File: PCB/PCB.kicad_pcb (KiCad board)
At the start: 4 copper layers, 54 x 29 mm, 108 parts, among them J1 USB_B_Micro, J2 Conn_01x02, Q1 PJA3428, Q2 PJA3428, Q3 AO3401A, SW1 SW_Push, SW2 SW_Push, SW3 SW_Push, SW4 ON/OFF, U1 ESP32-PICO-MINI-02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

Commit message: minor changes
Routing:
- net JTAG_TDI: track 0.00 -> 7.49 mm, vias 0 -> 1
- net JTAG_TDO: track 0.00 -> 5.23 mm, vias 0 -> 1
- net GPIO0: track 26.8 -> 27.6 mm
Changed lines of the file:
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@@
   (via (at 224.967457 102.491185) (size 0.8) (drill 0.4) (layers "F.Cu" "B.Cu") (net 8))
   (via (at 210.58 104.74) (size 0.8) (drill 0.4) (layers "F.Cu" "B.Cu") (net 8))
-  (segment (start 212.42 103.95) (end 211.81 103.95) (width 0.2) (layer "B.Cu") (net 8))
-  (segment (start 211.09 104.67) (end 211.02 104.74) (width 0.2) (layer "B.Cu") (net 8))
-  (segment (start 222.94 103.95) (end 212.42 103.95) (width 0.2) (layer "B.Cu") (net 8))
+  (segment (start 210.58 104.81) (end 211.479119 105.709119) (width 0.2) (layer "B.Cu") (net 8))
+  (segment (start 215.09387 104.16) (end 222.73 104.16) (width 0.2) (layer "B.Cu") (net 8))
+  (segment (start 210.58 104.74) (end 210.58 104.81) (width 0.2) (layer "B.Cu") (net 8))
+  (segment (start 211.479119 105.709119) (end 213.544751 105.709119) (width 0.2) (layer "B.Cu") (net 8))
   (segment (start 223.96 102.93) (end 224.528642 102.93) (width 0.2) (layer "B.Cu") (net 8))
   (segment (start 226.05 104.49) (end 225.52 104.49) (width 0.2) (layer "B.Cu") (net 8))
   (segment (start 224.528642 102.93) (end 224.967457 102.491185) (width 0.2) (layer "B.Cu") (net 8))
-  (segment (start 223.96 102.93) (end 223.27 103.62) (width 0.2) (layer "B.Cu") (net 8))
   (segment (start 225.52 104.49) (end 223.96 102.93) (width 0.2) (layer "B.Cu") (net 8))
-  (segment (start 223.27 103.62) (end 222.94 103.95) (width 0.2) (layer "B.Cu") (net 8))
-  (segment (start 211.02 104.74) (end 210.58 104.74) (width 0.2) (layer "B.Cu") (net 8))
-  (segment (start 211.81 103.95) (end 211.09 104.67) (width 0.2) (layer "B.Cu") (net 8))
+  (segment (start 213.544751 105.709119) (end 215.09387 104.16) (width 0.2) (layer "B.Cu") (net 8))
+  (segment (start 222.73 104.16) (end 223.96 102.93) (width 0.2) (layer "B.Cu") (net 8))
   (segment (start 228.785 106.13) (end 227.435 107.48) (width 0.2) (layer "B.Cu") (net 9))
   (segment (start 227.985 109.105) (end 228.485 109.105) (width 0.2) (layer "B.Cu") (net 9))
@@
   (segment (start 193.975 117.405) (end 193.28 118.1) (width 0.2) (layer "B.Cu") (net 87))
   (segment (start 193.975 116.85) (end 193.975 117.405) (width 0.2) (layer "B.Cu") (net 87))
+  (segment (start 213.79 103.4225) (end 213.79 104.394307) (width 0.2) (layer "F.Cu") (net 88))
+  (segment (start 213.79 104.394307) (end 213.175188 105.009119) (width 0.2) (layer "F.Cu") (net 88))
+  (via (at 213.175188 105.009119) (size 0.8) (drill 0.4) (layers "F.Cu" "B.Cu") (net 88))
+  (segment (start 213.8 104.107107) (end 213.888554 104.018554) (width 0.2) (layer "B.Cu") (net 88))
+  (segment (start 213.888554 104.018554) (end 215.245 102.662107) (width 0.2) (layer "B.Cu") (net 88))
+  (segment (start 213.175188 105.009119) (end 213.175188 104.73192) (width 0.2) (layer "B.Cu") (net 88))
+  (segment (start 213.175188 104.73192) (end 213.888554 104.018554) (width 0.2) (layer "B.Cu") (net 88))
+  (segment (start 215.245 101.33) (end 214.545 100.63) (width 0.2) (layer "B.Cu") (net 88))
+  (segment (start 215.245 102.662107) (end 215.245 101.33) (width 0.2) (layer "B.Cu") (net 88))
   (segment (start 212.99 102.275) (end 214.515 100.75) (width 0.2) (layer "F.Cu") (net 89))
   (segment (start 212.99 103.4225) (end 212.99 102.275) (width 0.2) (layer "F.Cu") (net 89))
@@
   (segment (start 215.215 99.92) (end 214.515 99.22) (width 0.2) (layer "F.Cu") (net 90))
   (segment (start 214.59 101.857107) (end 215.215 101.232107) (width 0.2) (layer "F.Cu") (net 90))
+  (segment (start 212.19 104.78) (end 212.2 104.79) (width 0.2) (layer "F.Cu") (net 91))
+  (segment (start 212.19 103.4225) (end 212.19 104.78) (width 0.2) (layer "F.Cu") (net 91))
+  (via (at 212.2 104.79) (size 0.8) (drill 0.4) (layers "F.Cu" "B.Cu") (net 91))
+  (segment (start 214.077107 102.18) (end 214.545 102.18) (width 0.2) (layer "B.Cu") (net 91))
+  (segment (start 212.2 104.79) (end 212.2 104.057107) (width 0.2) (layer "B.Cu") (net 91))
+  (segment (start 212.2 104.057107) (end 214.077107 102.18) (width 0.2) (layer "B.Cu") (net 91))
   (segment (start 212.432547 101.092453) (end 211.422453 101.092453) (width 0.2) (layer "B.Cu") (net 92))
   (segment (start 192.77 101.1) (end 192.77 100.3) (width 0.2) (layer "B.Cu") (net 92))

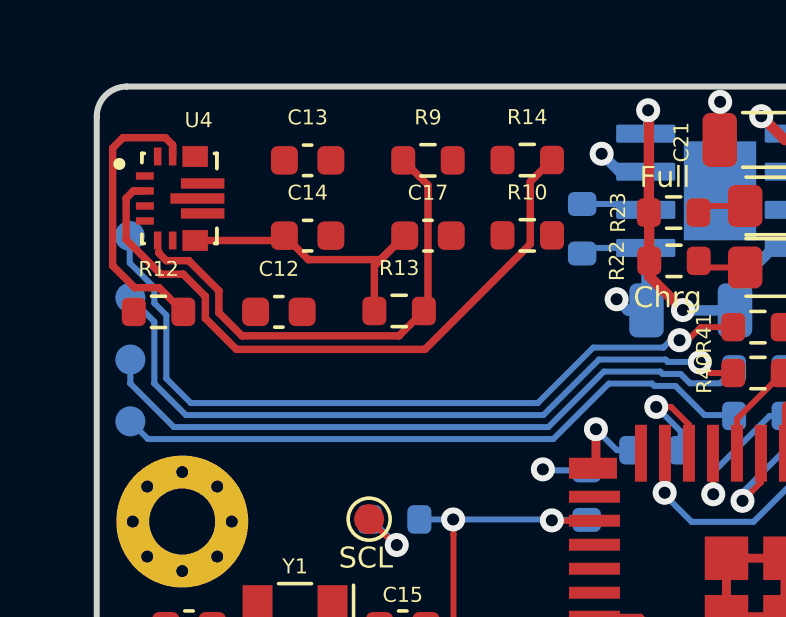
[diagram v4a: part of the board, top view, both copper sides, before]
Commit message: buck-boost pcb
layout updated
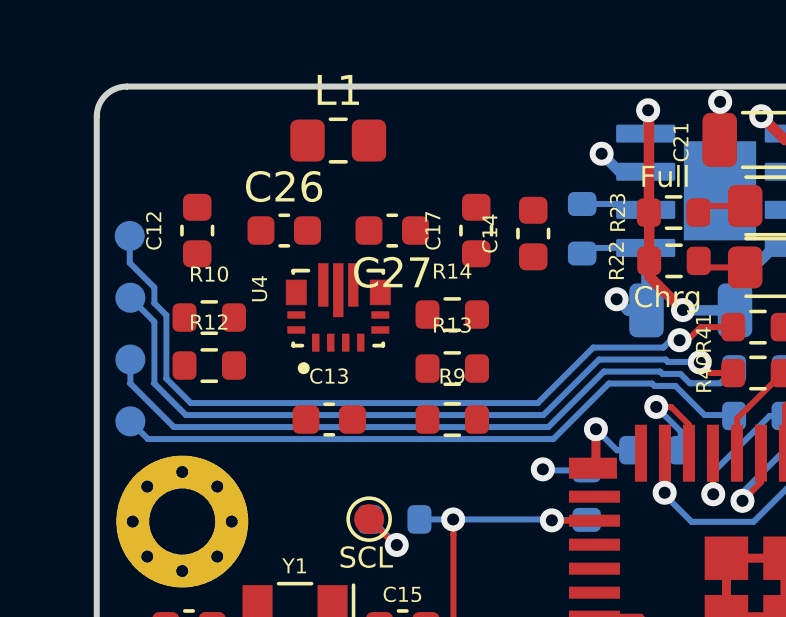
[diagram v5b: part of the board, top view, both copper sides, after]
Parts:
- added C26: 10uF, Capacitor_SMD:C_0603_1608Metric, F.Cu at (197.9, 96.0)
- added C27: 100nF, Capacitor_SMD:C_0603_1608Metric, F.Cu at (201.5, 96.0)
- added L1: L, Inductor_SMD:L_0805_2012Metric_Pad1.15x1.40mm_HandSolder, F.Cu at (199.7, 93.0)
- C13: value 100nF -> 10uF
- moved R10 10.9 mm to (195.4, 98.9)
- moved R9 8.68 mm to (203.5, 102.3)
- moved C13 8.67 mm to (199.4, 102.3)
- moved C14 7.52 mm to (206.2, 96.1), turned to 90 degrees
- moved U4 6.44 mm to (199.7, 98.6), turned to 90 degrees
- moved R14 5.72 mm to (203.5, 98.8)
- moved C12 3.84 mm to (195.0, 96.0), turned to 90 degrees
- moved R13 2.61 mm to (203.5, 100.6)
- moved R12 2.46 mm to (195.4, 100.5)
- moved C17 1.62 mm to (204.3, 96.0), turned to 90 degrees
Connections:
- C12 pad 1: GND -> Net-(C12-Pad1)
- R10 pad 1: GND -> Net-(C12-Pad1)
- U4 pad 1: GND -> Net-(C12-Pad1)
- U4 pad 12_13: GND -> Net-(C12-Pad1)
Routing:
- net Net-(R14-Pad2): track 22.1 -> 0.00 mm
- net Net-(R13-Pad2): track 16.2 -> 0.00 mm
- net Net-(C14-Pad1): track 10.6 -> 0.00 mm
- net Net-(R10-Pad2): track 9.54 -> 0.00 mm

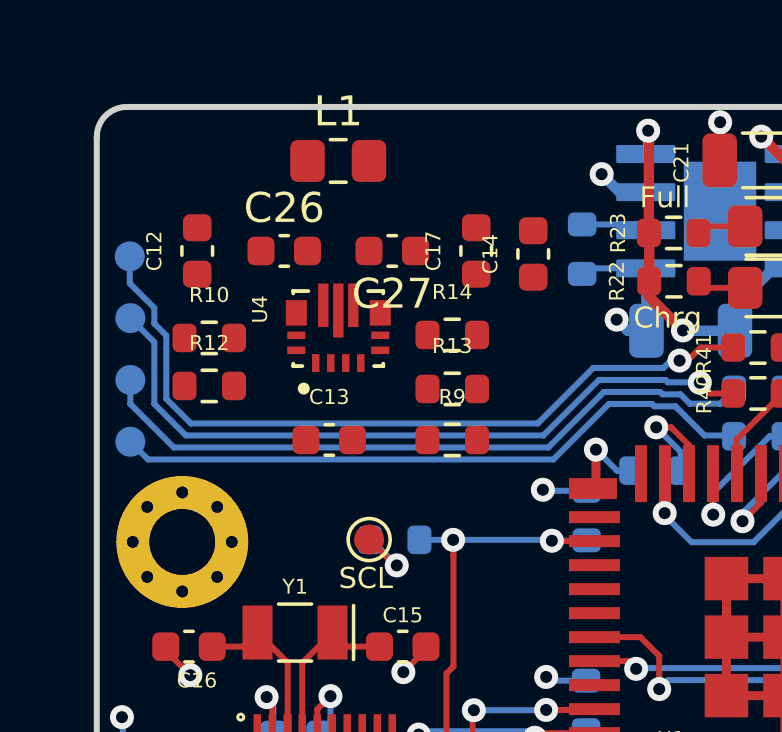
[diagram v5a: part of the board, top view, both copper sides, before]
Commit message: buck-boost layout
changed to layout from TI Web bench
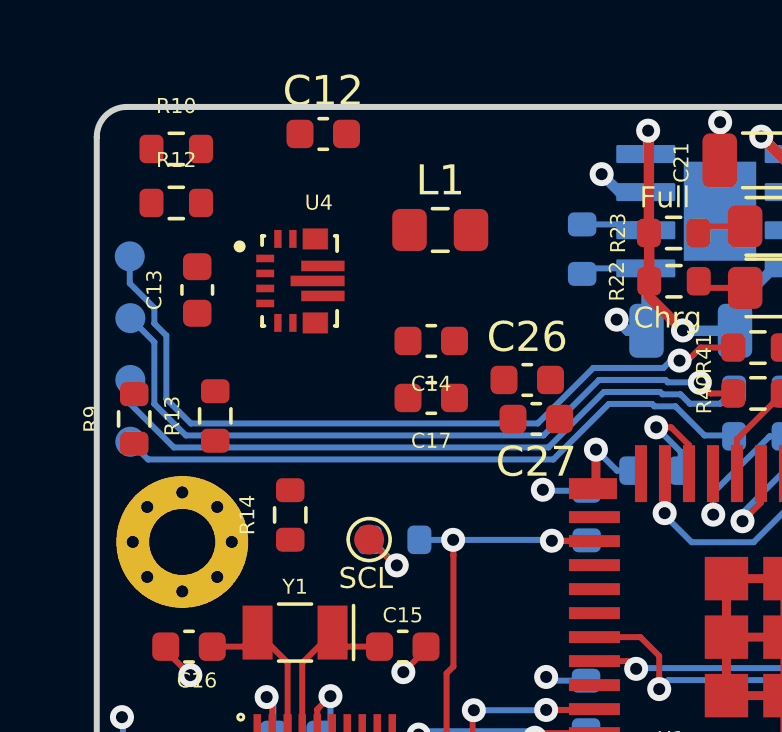
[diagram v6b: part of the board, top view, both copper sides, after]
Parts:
- moved R9 10.6 mm to (192.9, 101.6), turned to 90 degrees
- moved C26 9.17 mm to (206.0, 100.3)
- moved R14 8.07 mm to (198.1, 104.8), turned to 90 degrees
- moved R13 7.95 mm to (195.6, 101.5), turned to 90 degrees
- moved C27 7.38 mm to (206.3, 101.6)
- moved C13 6.66 mm to (195.0, 97.3), turned to 90 degrees
- moved R10 6.40 mm to (194.3, 92.6)
- moved R12 6.20 mm to (194.3, 94.4)
- moved C12 5.73 mm to (199.2, 92.1), turned to 0 degrees
- moved C17 5.12 mm to (202.8, 100.9), turned to 180 degrees
- moved C14 4.47 mm to (202.8, 99.0), turned to 180 degrees
- moved L1 4.10 mm to (203.1, 95.3)
- moved U4 2.04 mm to (198.4, 97.0), turned to 0 degrees

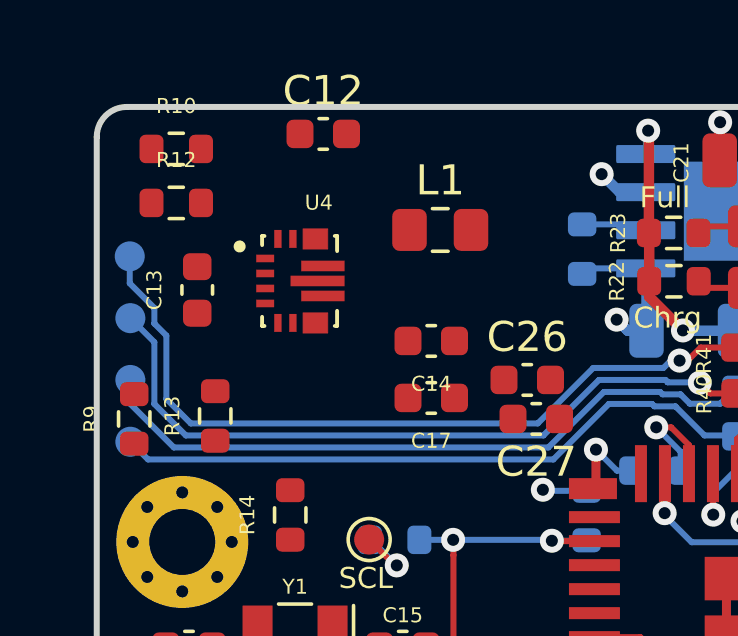
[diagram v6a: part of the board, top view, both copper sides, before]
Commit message: buck-boost edits
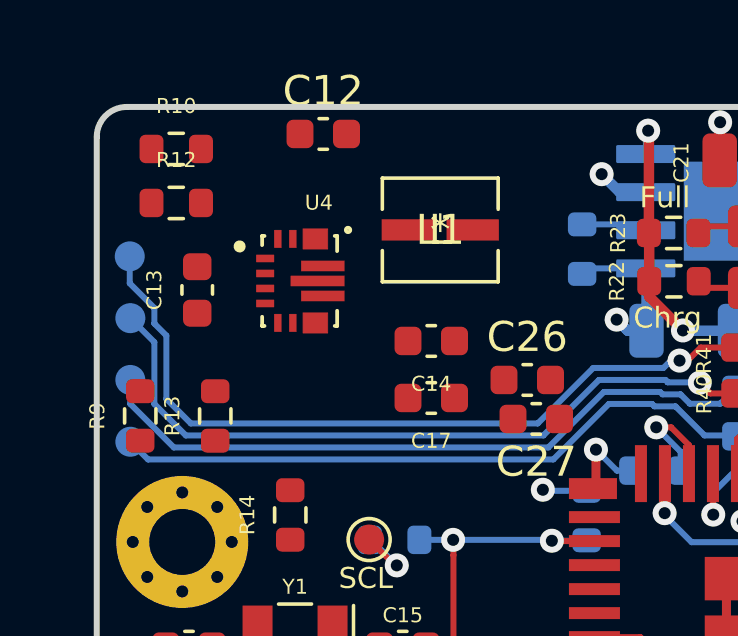
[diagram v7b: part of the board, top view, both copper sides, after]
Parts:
- L1: footprint Inductor_SMD:L_0805_2012Metric_Pad1.15x1.40mm_HandSolder -> inductor:IHLP1212BZERR56M11
- moved R9 0.22 mm to (193.1, 101.5)
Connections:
- C12 pad 1: Net-(C26-Pad1) -> Vin
- C26 pad 1: Net-(C26-Pad1) -> Vin
- R10 pad 1: Net-(C26-Pad1) -> Vin
- U4 pad 1: Net-(C26-Pad1) -> Vin
- U4 pad 12_13: Net-(C26-Pad1) -> Vin
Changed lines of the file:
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@@
   (net 94 "Net-(R41-Pad1)")
   (net 95 "Net-(R42-Pad1)")
-  (net 96 "Net-(C26-Pad1)")
   (footprint "Capacitor_SMD:C_0603_1608Metric" (layer "F.Cu")
     (at 206 100.3)
@@
     (fp_line (start 0.8 0.4) (end -0.8 0.4) (layer "F.Fab") (width 0.1))
     (pad "1" smd roundrect (at -0.775 0) (size 0.9 0.95) (layers "F.Cu" "F.Paste" "F.Mask") (roundrect_rratio 0.25)
-      (net 96 "Net-(C26-Pad1)") (pintype "passive"))
+      (net 26 "Vin") (pintype "passive"))
     (pad "2" smd roundrect (at 0.775 0) (size 0.9 0.95) (layers "F.Cu" "F.Paste" "F.Mask") (roundrect_rratio 0.25)
       (net 71 "GND") (pintype "passive"))
@@
     (fp_line (start 0.8 -0.4125) (end 0.8 0.4125) (layer "F.Fab") (width 0.1))
     (pad "1" smd roundrect (at -0.825 0) (size 0.8 0.95) (layers "F.Cu" "F.Paste" "F.Mask") (roundrect_rratio 0.25)
-      (net 96 "Net-(C26-Pad1)") (pintype "passive"))
+      (net 26 "Vin") (pintype "passive"))
     (pad "2" smd roundrect (at 0.825 0) (size 0.8 0.95) (layers "F.Cu" "F.Paste" "F.Mask") (roundrect_rratio 0.25)
       (net 74 "Net-(R10-Pad2)") (pintype "passive"))
@@
   )
   (footprint "Resistor_SMD:R_0603_1608Metric" (layer "F.Cu")
-    (at 192.9 101.6 90)
+    (at 193.1 101.5 90)
     (descr "Resistor SMD 0603 (1608 Metric), square (rectangular) end terminal, IPC_7351 nominal, (Body size source: IPC-SM-782 page 72, https://www.pcb-3d.com/wordpress/wp-content/uploads/ipc-sm-782a_amendment_1_and_2.pdf), generated with kicad-footprint-generator")
     (tags "resistor")
@@
     (fp_circle (center -2 -1.15) (end -1.9 -1.15) (layer "F.Fab") (width 0.2) (fill none))
     (pad "1" smd roundrect locked (at -1.15 -0.75) (size 0.6 0.25) (layers "F.Cu" "F.Paste") (roundrect_rratio 0.01)
-      (net 96 "Net-(C26-Pad1)") (pinfunction "PS/SYNC") (pintype "input"))
+      (net 26 "Vin") (pinfunction "PS/SYNC") (pintype "input"))
     (pad "2" smd roundrect locked (at -1.15 -0.25) (size 0.6 0.25) (layers "F.Cu" "F.Paste") (roundrect_rratio 0.01)
       (net 75 "Net-(R14-Pad2)") (pinfunction "PG") (pintype "output"))
@@
       (net 76 "Net-(L1-Pad1)") (pinfunction "L1") (pintype "bidirectional"))
     (pad "12_13" smd roundrect locked (at 0.525 -1.4) (size 0.85 0.7) (layers "F.Cu") (roundrect_rratio 0.02)
-      (net 96 "Net-(C26-Pad1)") (pinfunction "VIN") (pintype "input"))
+      (net 26 "Vin") (pinfunction "VIN") (pintype "input"))
     (pad "14" smd roundrect locked (at -0.225 -1.4) (size 0.25 0.6) (layers "F.Cu" "F.Paste") (roundrect_rratio 0.01)
       (net 74 "Net-(R10-Pad2)") (pinfunction "EN") (pintype "input"))
@@
     )
   )
-  (footprint "Inductor_SMD:L_0805_2012Metric_Pad1.15x1.40mm_HandSolder" (layer "F.Cu")
+  (footprint "inductor:IHLP1212BZERR56M11" (layer "F.Cu")
     (at 203.1 95.3)
-    (descr "Inductor SMD 0805 (2012 Metric), square (rectangular) end terminal, IPC_7351 nominal with elongated pad for handsoldering. (Body size source: https://docs.google.com/spreadsheets/d/1BsfQQcO9C6DZCsRaXUlFlo91Tg2WpOkGARC1WS5S8t0/edit?usp=sharing), generated with kicad-footprint-generator")
-    (tags "inductor handsolder")
-    (property "Sheetfile" "PCB.kicad_sch")
-    (property "Sheetname" "")
-    (attr smd)
-    (fp_text reference "L1" (at 0 -1.65) (layer "F.SilkS")
-      (effects (font (size 1 1) (thickness 0.15)))
-    )
-    (fp_text value "L" (at 0 1.65) (layer "F.Fab")
-      (effects (font (size 1 1) (thickness 0.15)))
-    )
-    (fp_text user "${REFERENCE}" (at 0 0) (layer "F.Fab")
-      (effects (font (size 0.5 0.5) (thickness 0.08)))
-    )
-    (fp_line (start -0.261252 -0.71) (end 0.261252 -0.71) (layer "F.SilkS") (width 0.12))
-    (fp_line (start -0.261252 0.71) (end 0.261252 0.71) (layer "F.SilkS") (width 0.12))
-    (fp_line (start 1.85 -0.95) (end 1.85 0.95) (layer "F.CrtYd") (width 0.05))
-    (fp_line (start -1.85 -0.95) (end 1.85 -0.95) (layer "F.CrtYd") (width 0.05))
-    (fp_line (start 1.85 0.95) (end -1.85 0.95) (layer "F.CrtYd") (width 0.05))
-    (fp_line (start -1.85 0.95) (end -1.85 -0.95) (layer "F.CrtYd") (width 0.05))
-    (fp_line (start 1 -0.6) (end 1 0.6) (layer "F.Fab") (width 0.1))
-    (fp_line (start -1 -0.6) (end 1 -0.6) (layer "F.Fab") (width 0.1))
-    (fp_line (start -1 0.6) (end -1 -0.6) (layer "F.Fab") (width 0.1))
-    (fp_line (start 1 0.6) (end -1 0.6) (layer "F.Fab") (width 0.1))
-    (pad "1" smd roundrect (at -1.025 0) (size 1.15 1.4) (layers "F.Cu" "F.Paste" "F.Mask") (roundrect_rratio 0.217391)
+    (property "Sheetfile" "PCB.kicad_sch")
+    (property "Sheetname" "")
+    (attr through_hole)
+    (fp_text reference "L1" (at 0 0) (layer "F.SilkS")
+      (effects (font (size 1 1) (thickness 0.15)))
+    )
+    (fp_text value "L" (at 0 0) (layer "F.SilkS")
+      (effects (font (size 1 1) (thickness 0.15)))
+    )
+    (fp_text user "*" (at 0 0) (layer "F.SilkS")
+      (effects (font (size 1 1) (thickness 0.15)))
+    )
+    (fp_text user "Copyright 2021 Accelerated Designs. All rights reserved." (at 0 0) (layer "Cmts.User")
+      (effects (font (size 0.127 0.127) (thickness 0.002)))
+    )
+    (fp_text user "*" (at 0 0) (layer "F.Fab")
+      (effects (font (size 1 1) (thickness 0.15)))
+    )
+    (fp_line (start -1.9304 0.68834) (end -1.9304 1.7272) (layer "F.SilkS") (width 0.12))
+    (fp_line (start 1.9304 -0.68834) (end 1.9304 -1.7272) (layer "F.SilkS") (width 0.12))
+    (fp_line (start 1.9304 1.7272) (end 1.9304 0.68834) (layer "F.SilkS") (width 0.12))
+    (fp_line (start 1.9304 -1.7272) (end -1.9304 -1.7272) (layer "F.SilkS") (width 0.12))
+    (fp_line (start -1.9304 1.7272) (end 1.9304 1.7272) (layer "F.SilkS") (width 0.12))
+    (fp_line (start -1.9304 -1.7272) (end -1.9304 -0.68834) (layer "F.SilkS") (width 0.12))
+    (fp_circle (center -3.0734 0) (end -2.9972 0) (layer "F.SilkS") (width 0.12) (fill none))
+    (fp_line (start -2.0574 0.6096) (end -2.2074 0.6096) (layer "F.CrtYd") (width 0.05))
+    (fp_line (start -2.0574 -0.6096) (end -2.0574 -1.8542) (layer "F.CrtYd") (width 0.05))
+    (fp_line (start 2.0574 0.6096) (end 2.0574 1.8542) (layer "F.CrtYd") (width 0.05))
+    (fp_line (start -2.2074 0.6096) (end -2.2074 -0.6096) (layer "F.CrtYd") (width 0.05))
+    (fp_line (start 2.0574 -1.8542) (end 2.0574 -0.6096) (layer "F.CrtYd") (width 0.05))
+    (fp_line (start -2.0574 0.6096) (end -2.2074 0.6096) (layer "F.CrtYd") (width 0.05))
+    (fp_line (start 2.0574 0.6096) (end 2.0574 1.8542) (layer "F.CrtYd") (width 0.05))
+    (fp_line (start 2.2074 -0.6096) (end 2.2074 0.6096) (layer "F.CrtYd") (width 0.05))
+    (fp_line (start 2.0574 -1.8542) (end 2.0574 -0.6096) (layer "F.CrtYd") (width 0.05))
+    (fp_line (start 2.0574 1.8542) (end -2.0574 1.8542) (layer "F.CrtYd") (width 0.05))
+    (fp_line (start -2.0574 1.8542) (end -2.0574 0.6096) (layer "F.CrtYd") (width 0.05))
+    (fp_line (start 2.2074 -0.6096) (end 2.2074 0.6096) (layer "F.CrtYd") (width 0.05))
+    (fp_line (start -2.2074 0.6096) (end -2.2074 -0.6096) (layer "F.CrtYd") (width 0.05))
+    (fp_line (start 2.2074 0.6096) (end 2.0574 0.6096) (layer "F.CrtYd") (width 0.05))
+    (fp_line (start -2.2074 -0.6096) (end -2.0574 -0.6096) (layer "F.CrtYd") (width 0.05))
+    (fp_line (start 2.0574 1.8542) (end -2.0574 1.8542) (layer "F.CrtYd") (width 0.05))
+    (fp_line (start -2.0574 -1.8542) (end 2.0574 -1.8542) (layer "F.CrtYd") (width 0.05))
+    (fp_line (start 2.2074 0.6096) (end 2.0574 0.6096) (layer "F.CrtYd") (width 0.05))
+    (fp_line (start -2.0574 -1.8542) (end 2.0574 -1.8542) (layer "F.CrtYd") (width 0.05))
+    (fp_line (start -2.2074 -0.6096) (end -2.0574 -0.6096) (layer "F.CrtYd") (width 0.05))
+    (fp_line (start -2.0574 -0.6096) (end -2.0574 -1.8542) (layer "F.CrtYd") (width 0.05))
+    (fp_line (start -2.0574 1.8542) (end -2.0574 0.6096) (layer "F.CrtYd") (width 0.05))
+    (fp_line (start 2.0574 -0.6096) (end 2.2074 -0.6096) (layer "F.CrtYd") (width 0.05))
+    (fp_line (start 2.0574 -0.6096) (end 2.2074 -0.6096) (layer "F.CrtYd") (width 0.05))
+    (fp_line (start 1.8034 -1.6002) (end -1.8034 -1.6002) (layer "F.Fab") (width 0.1))
+    (fp_line (start 1.8034 1.6002) (end 1.8034 -1.6002) (layer "F.Fab") (width 0.1))
+    (fp_line (start -1.8034 1.6002) (end 1.8034 1.6002) (layer "F.Fab") (width 0.1))
+    (fp_line (start -1.8034 -1.6002) (end -1.8034 1.6002) (layer "F.Fab") (width 0.1))
+    (fp_circle (center -1.2954 0) (end -1.2192 0) (layer "F.Fab") (width 0.1) (fill none))
+    (pad "1" smd rect (at -1.082301 0 90) (size 0.7112 1.742199) (layers "F.Cu" "F.Paste" "F.Mask")
       (net 76 "Net-(L1-Pad1)") (pinfunction "1") (pintype "passive"))
-    (pad "2" smd roundrect (at 1.025 0) (size 1.15 1.4) (layers "F.Cu" "F.Paste" "F.Mask") (roundrect_rratio 0.217391)
+    (pad "2" smd rect (at 1.082301 0 90) (size 0.7112 1.742199) (layers "F.Cu" "F.Paste" "F.Mask")
       (net 77 "Net-(L1-Pad2)") (pinfunction "2") (pintype "passive"))
-    (model "${KICAD6_3DMODEL_DIR}/Inductor_SMD.3dshapes/L_0805_2012Metric.wrl"
-      (offset (xyz 0 0 0))
-      (scale (xyz 1 1 1))
-      (rotate (xyz 0 0 0))
-    )
   )
   (footprint "Diode_SMD:D_1206_3216Metric" (layer "F.Cu")
@@
     (fp_line (start 0.8 -0.4) (end 0.8 0.4) (layer "F.Fab") (width 0.1))
     (pad "1" smd roundrect (at -0.775 0) (size 0.9 0.95) (layers "F.Cu" "F.Paste" "F.Mask") (roundrect_rratio 0.25)
-      (net 96 "Net-(C26-Pad1)") (pintype "passive"))
+      (net 26 "Vin") (pintype "passive"))
     (pad "2" smd roundrect (at 0.775 0) (size 0.9 0.95) (layers "F.Cu" "F.Paste" "F.Mask") (roundrect_rratio 0.25)
       (net 71 "GND") (pintype "passive"))
